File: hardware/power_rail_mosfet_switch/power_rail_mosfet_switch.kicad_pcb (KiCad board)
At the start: 2 copper layers, 42 x 12 mm, 8 parts, among them J1 Screw_Terminal_01x03, J2 Screw_Terminal_01x02, Q1 HXY2102EI, Q2 AO3401A

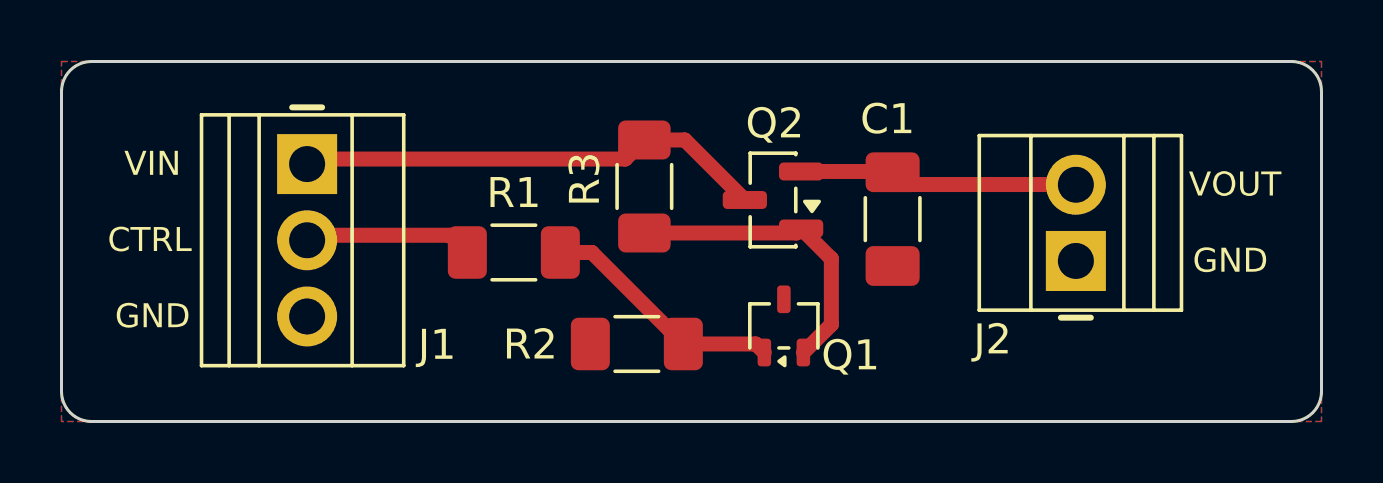
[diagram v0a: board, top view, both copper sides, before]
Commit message: set label text size
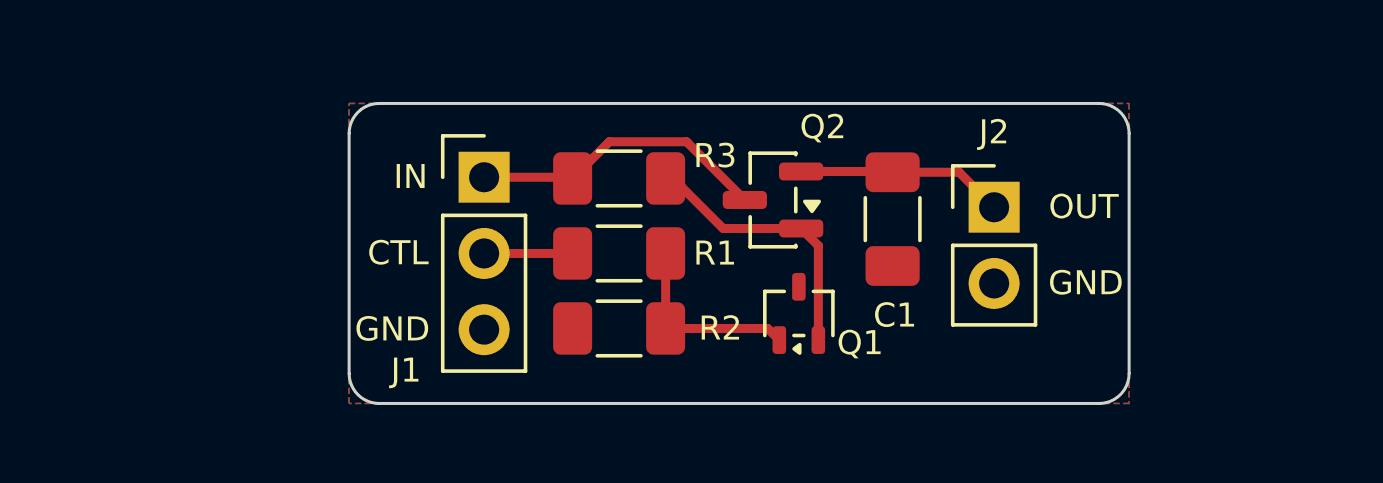
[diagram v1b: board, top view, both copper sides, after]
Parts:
- J1: value Screw_Terminal_01x03 -> Conn_01x03_Pin; footprint Connectors:Toponelec_TY308-2.54-03P-14-00AH_1x03_P2.54mm_Horizontal -> Connector_PinHeader_2.54mm:PinHeader_1x03_P2.54mm_Vertical
- J2: value Screw_Terminal_01x02 -> Conn_01x02_Pin; footprint Connectors:Toponelec_TY308-2.54-02P-14-00AH_1x02_P2.54mm_Horizontal -> Connector_PinHeader_2.54mm:PinHeader_1x02_P2.54mm_Vertical
- moved J1 5.92 mm to (133.0, 54.0), turned to 0 degrees
- moved R1 3.51 mm to (137.5, 56.5)
- moved J2 3.26 mm to (150.0, 55.0), turned to 0 degrees
- moved R3 0.88 mm to (137.5, 54.0), turned to 0 degrees
- moved R2 0.79 mm to (137.5, 59.0)
- moved Q1 0.65 mm to (143.5, 58.5)
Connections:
- C1 pad 1: Net-(J2-Pin_2) -> Net-(J2-Pin_1)
- J2 pad 1: GND -> Net-(J2-Pin_1)
- J2 pad 2: Net-(J2-Pin_2) -> GND
- Q2 pad 2: Net-(J2-Pin_2) -> Net-(J2-Pin_1)
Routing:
- net Net-(J2-Pin_2): track 9.63 -> 0.00 mm
- net Net-(J2-Pin_1): track 0.00 -> 6.93 mm
- net Net-(J1-Pin_1): track 15.8 -> 10.0 mm
- net Net-(J1-Pin_2): track 5.70 -> 2.95 mm
- net Net-(Q1-G): track 8.18 -> 6.45 mm
- net Net-(Q1-D): track 10.2 -> 9.17 mm
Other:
- board size 42 x 12 mm -> 26 x 10 mm
- board text added: "C"
- board text added: "CTL"
- board text added: "G"
- board text added: "I"
- board text added: "IN"
- board text added: "O"
- board text added: "OUT"
- board text removed: "CTRL"
- board text removed: "VIN"
- board text removed: "VOUT"

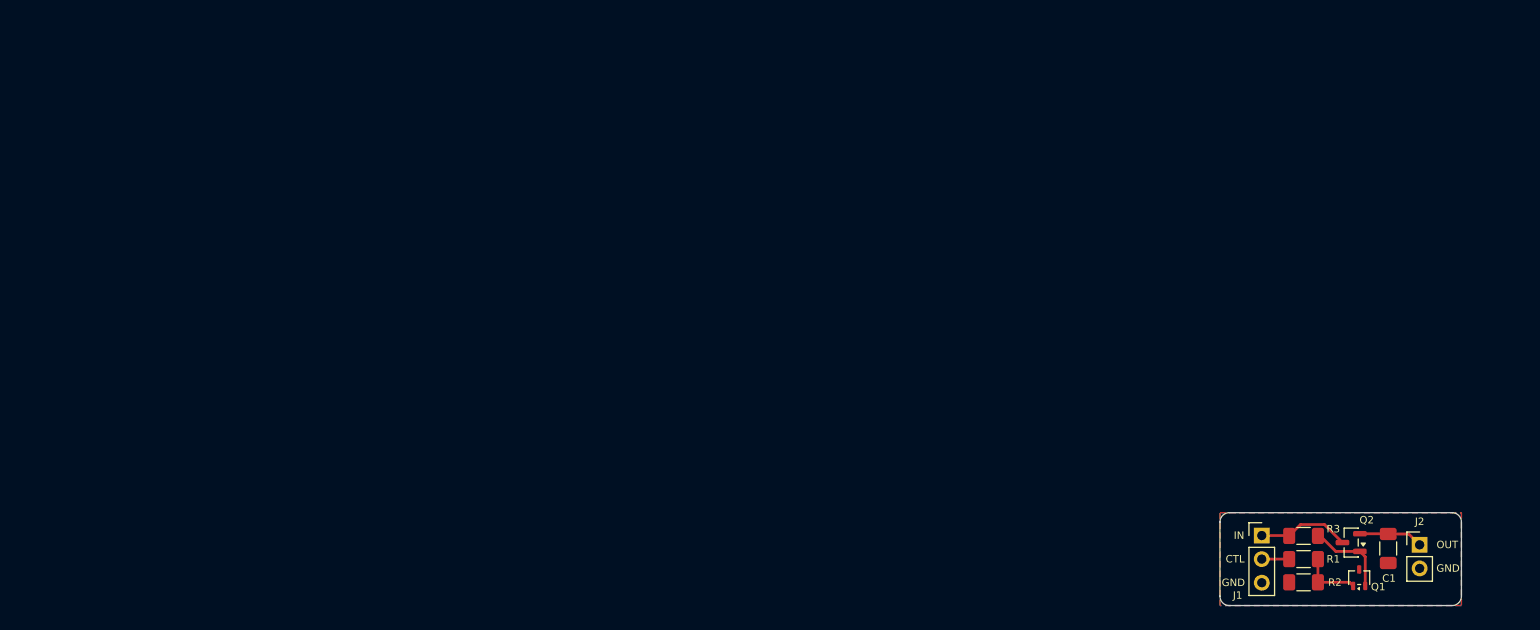
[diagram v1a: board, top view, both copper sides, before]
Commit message: Update footprints
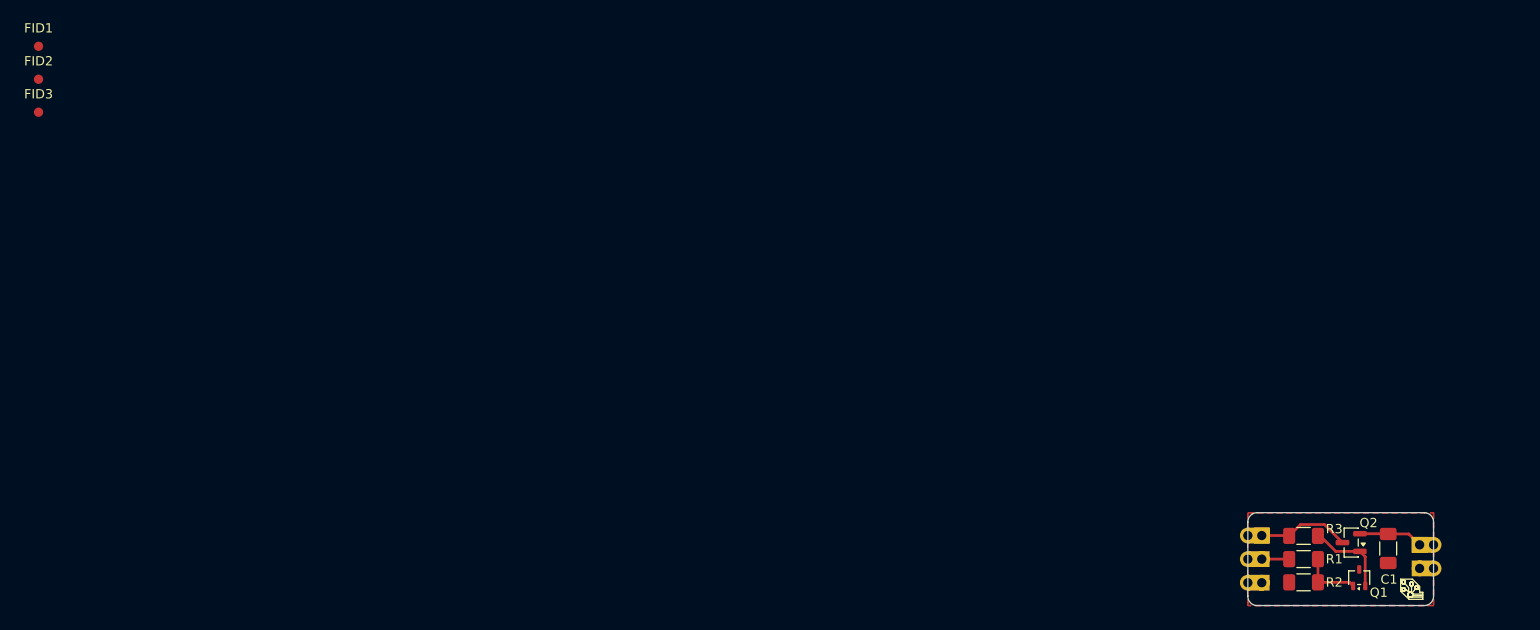
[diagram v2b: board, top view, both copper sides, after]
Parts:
- added FID1: Fiducial, Fiducial:Fiducial_1mm_Mask2mm, F.Cu at (1.27, 1.27)
- added FID2: Fiducial, Fiducial:Fiducial_1mm_Mask2mm, F.Cu at (1.27, 4.83)
- added FID3: Fiducial, Fiducial:Fiducial_1mm_Mask2mm, F.Cu at (1.27, 8.38)
- J1: footprint Connector_PinHeader_2.54mm:PinHeader_1x03_P2.54mm_Vertical -> Mekatrol_Footprints:PinHeader_1x03_P2.54mm_With_Left_Castellations
- J2: footprint Connector_PinHeader_2.54mm:PinHeader_1x02_P2.54mm_Vertical -> Mekatrol_Footprints:PinHeader_1x02_P2.54mm_With_Right_Castellations
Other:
- board size 26 x 10 mm -> 20 x 10 mm
- board text added: "CTRL"
- board text added: "PWR SWITCH v1.0"
- board text added: "SEP 2026"
- board text added: "VIN"
- board text added: "VOUT"
- board text removed: "C"
- board text removed: "CTL"
- board text removed: "G"
- board text removed: "I"
- board text removed: "IN"
- board text removed: "O"
- board text removed: "OUT"
- board text removed: "Power Switch V1.0"
- board text removed: "Sep 2026"

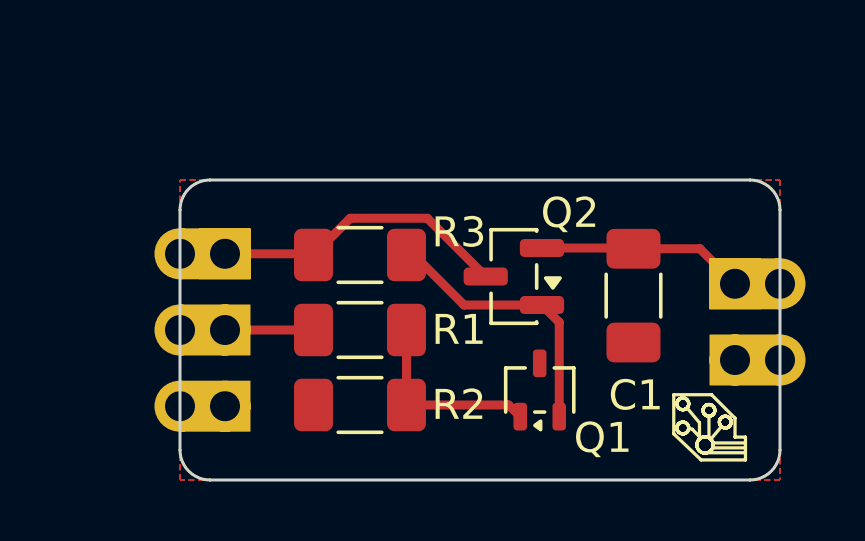
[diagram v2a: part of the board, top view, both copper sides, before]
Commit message: Fix zone priority
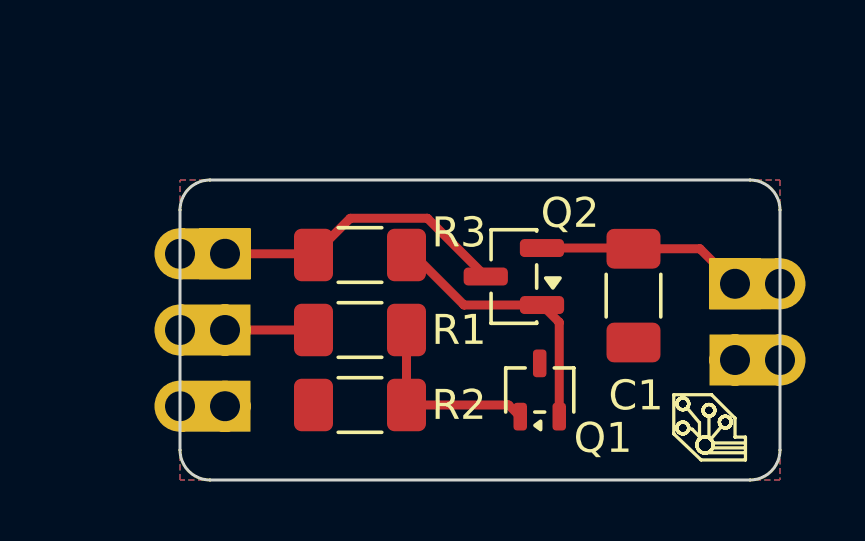
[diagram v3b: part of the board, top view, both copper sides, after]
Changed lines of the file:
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@@
 		(sheetname "/")
 		(sheetfile "power_rail_mosfet_switch.kicad_sch")
-		(units
-			(unit
-				(name "A")
-				(pins "1" "2")
-			)
-		)
 		(attr through_hole)
 		(duplicate_pad_numbers_are_jumpers no)
@@
 		(sheetname "/")
 		(sheetfile "power_rail_mosfet_switch.kicad_sch")
-		(units
-			(unit
-				(name "A")
-				(pins "1" "2" "3")
-			)
-		)
 		(attr through_hole)
 		(duplicate_pad_numbers_are_jumpers no)
@@
 		(net "GND")
 		(layer "F.Cu")
-		(name "GND")
+		(name "GND_FRONT")
 		(hatch edge 0.5)
 		(connect_pads
@@
 			(thermal_gap 0.2)
 			(thermal_bridge_width 0.3)
+			(smoothing fillet)
 			(island_removal_mode 0)
 		)
@@
 	(zone
 		(net "GND")
-		(layers "F.Cu" "B.Cu")
-		(name "GND_1")
+		(layer "B.Cu")
+		(name "GND_BACK")
 		(hatch edge 0.5)
 		(connect_pads

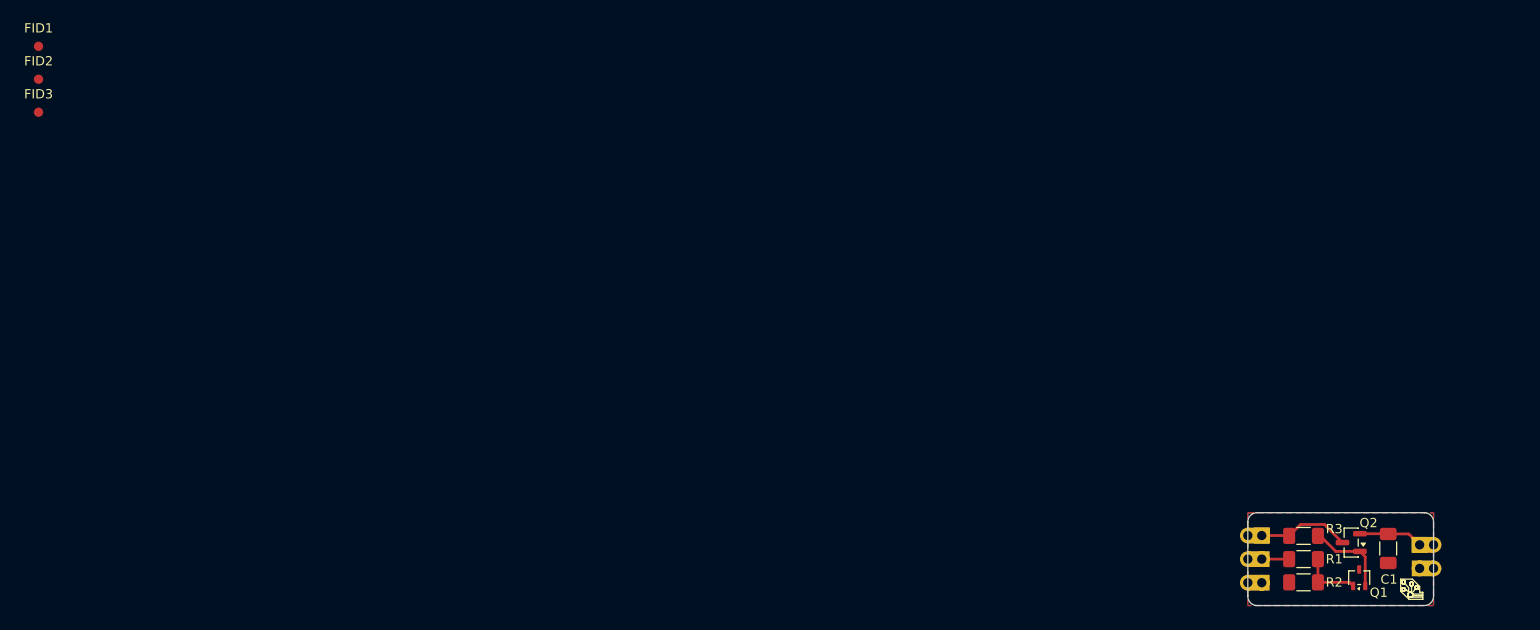
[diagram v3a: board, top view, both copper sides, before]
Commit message: Update footprint to kicad 10
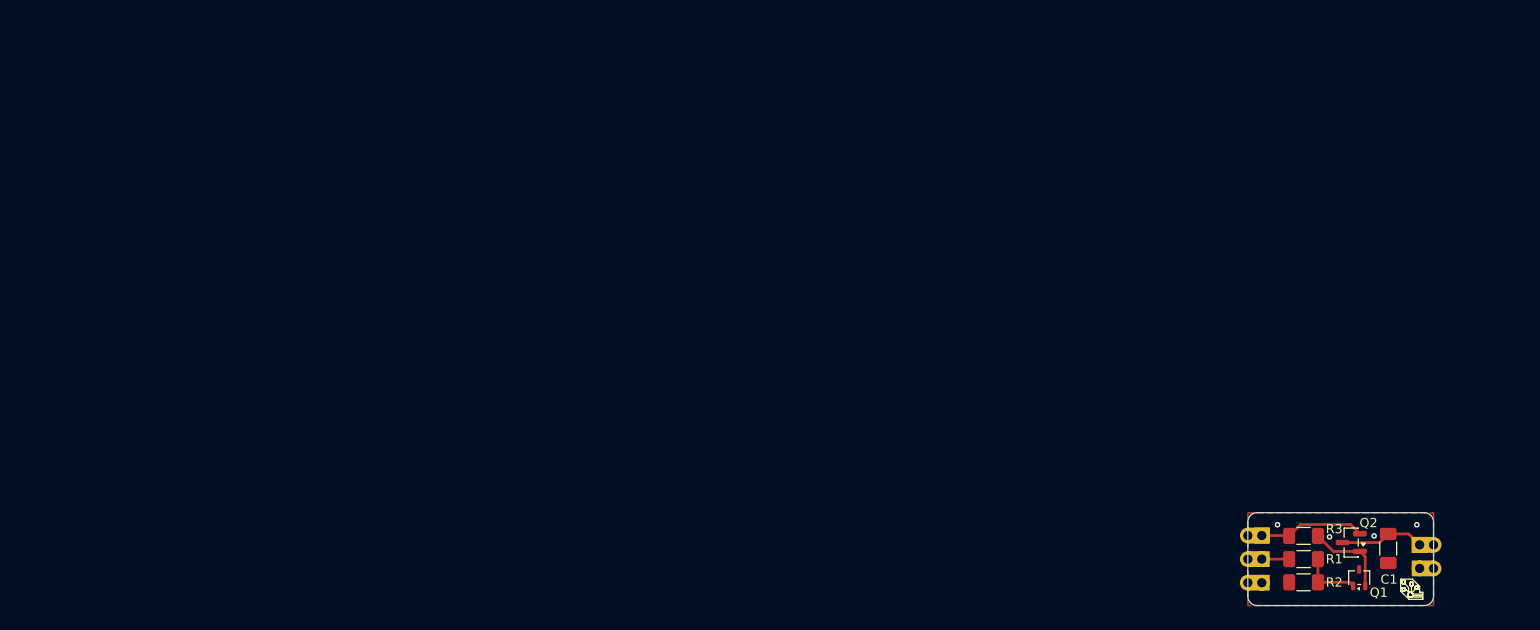
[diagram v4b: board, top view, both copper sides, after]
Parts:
- removed FID1, FID2, FID3: Fiducial, Fiducial:Fiducial_1mm_Mask2mm
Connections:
- net Net-(J1-Pin_2) renamed /CTRL
- C1 pad 1: Net-(J2-Pin_1) -> /VOUT
- J1 pad 1: Net-(J1-Pin_1) -> /VIN
- J2 pad 1: Net-(J2-Pin_1) -> /VOUT
- Q2 pad 2: Net-(J2-Pin_1) -> /VIN
- Q2 pad 3: Net-(J1-Pin_1) -> /VOUT
- R3 pad 1: Net-(J1-Pin_1) -> /VIN
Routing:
- net /VIN: track 0.00 -> 11.5 mm
- net Net-(J1-Pin_1): track 10.0 -> 0.00 mm
- net /VOUT: track 0.00 -> 9.18 mm
- net Net-(J2-Pin_1): track 6.93 -> 0.00 mm
- net GND: vias 0 -> 4
